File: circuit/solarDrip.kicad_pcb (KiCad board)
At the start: 2 copper layers, 57 x 50 mm, 51 parts, among them J1 solar_charger, J10 Conn_01x08_Socket, J11 Logo_bot, J12 Logo_µc3, J13 solar_charger_smd, J2 batt, J3 solar, J4 pump, J5 soil, J6 water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

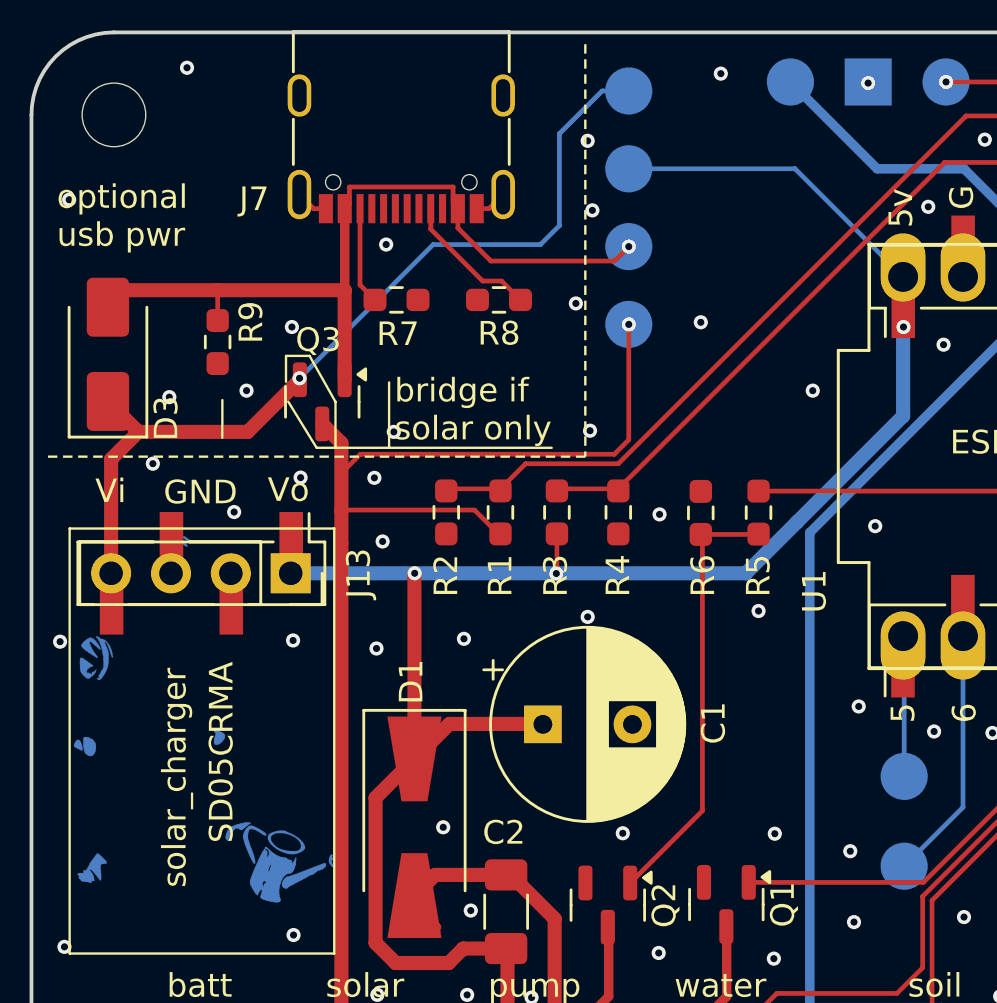
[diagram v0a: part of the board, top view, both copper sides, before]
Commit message: fix usb net
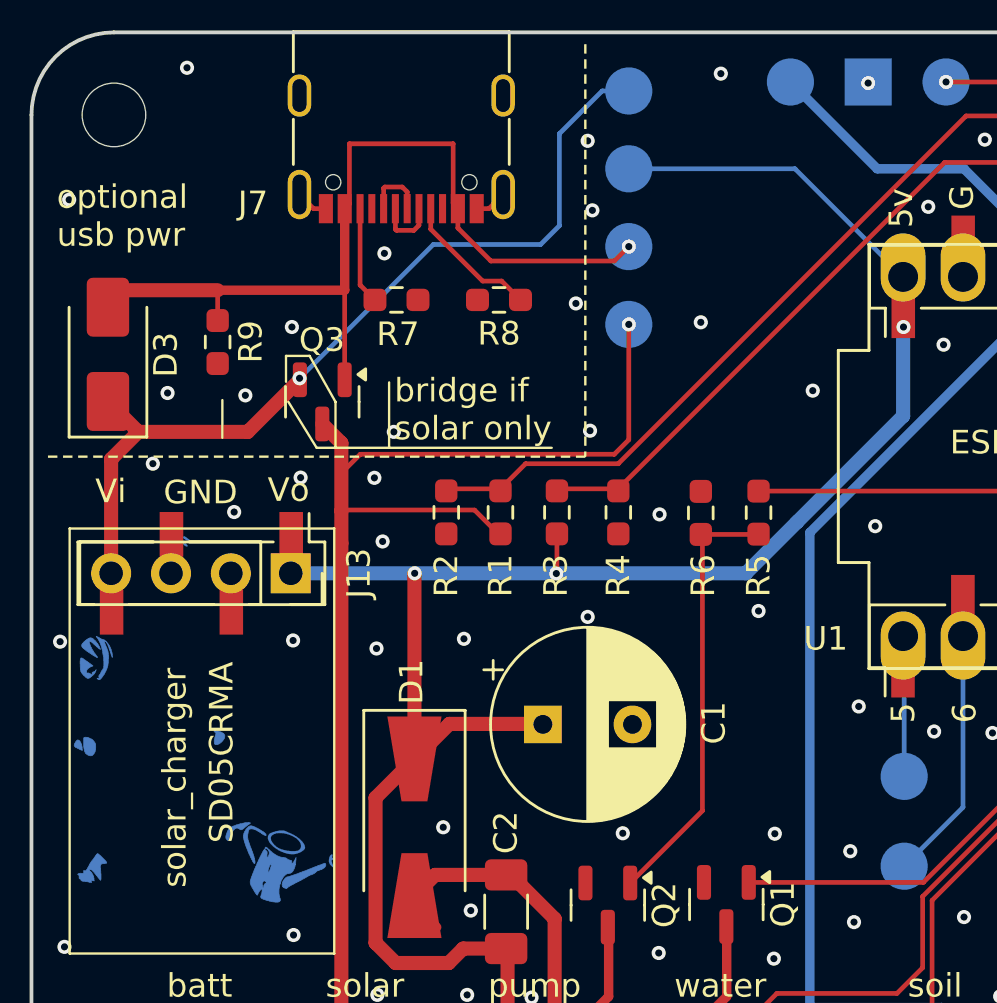
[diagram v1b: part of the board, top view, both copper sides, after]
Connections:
- J7 pad A6: unconnected-(J7-D+-PadA6) -> Net-(J7-D+-PadA6)
- J7 pad A7: unconnected-(J7-D--PadA7) -> Net-(J7-D--PadA7)
- J7 pad B6: unconnected-(J7-D+-PadB6) -> Net-(J7-D+-PadA6)
- J7 pad B7: unconnected-(J7-D--PadB7) -> Net-(J7-D--PadA7)
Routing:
- net vcc_usb: track 34.2 -> 37.9 mm
- net Net-(J7-D+-PadA6): track 0.00 -> 2.69 mm
- net Net-(J7-D--PadA7): track 0.00 -> 2.68 mm
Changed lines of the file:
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@@
 	(net 22 "gpio21")
 	(net 23 "Net-(J7-CC1)")
-	(net 24 "unconnected-(J7-D+-PadA6)")
-	(net 25 "unconnected-(J7-D--PadB7)")
-	(net 26 "unconnected-(J7-D--PadA7)")
-	(net 27 "unconnected-(J7-D+-PadB6)")
-	(net 28 "Net-(J7-CC2)")
+	(net 24 "Net-(J7-D+-PadA6)")
+	(net 25 "Net-(J7-D--PadA7)")
+	(net 26 "Net-(J7-CC2)")
 	(footprint "TestPoint:TestPoint_Pad_2.0x2.0mm"
 		(layer "F.Cu")
@@
 		(tags "SOT TO_SOT_SMD")
 		(property "Reference" "Q3"
-			(at -2.625 0.1642 180)
+			(at -2.625 0.0142 180)
 			(layer "F.SilkS")
 			(effects
@@
 		(property "Value" "pump"
 			(at 1.15 -2.75 0)
-			(layer "F.SilkS")
+			(layer "F.SilkS" knockout)
 			(effects
 				(font
@@
 		(tags "USB C Type-C Receptacle SMD")
 		(property "Reference" "J7"
-			(at 6.242 -3.321 180)
+			(at 6.292 -3.496 180)
 			(layer "F.SilkS")
 			(effects
@@
 			(size 0.3 1.24)
 			(layers "F.Cu" "F.Paste" "F.Mask")
-			(net 24 "unconnected-(J7-D+-PadA6)")
+			(net 24 "Net-(J7-D+-PadA6)")
 			(pinfunction "D+")
-			(pintype "bidirectional+no_connect")
+			(pintype "bidirectional")
 		)
 		(pad "A7" smd rect
@@
 			(size 0.3 1.24)
 			(layers "F.Cu" "F.Paste" "F.Mask")
-			(net 26 "unconnected-(J7-D--PadA7)")
+			(net 25 "Net-(J7-D--PadA7)")
 			(pinfunction "D-")
-			(pintype "bidirectional+no_connect")
+			(pintype "bidirectional")
 		)
 		(pad "A8" smd rect
@@
 			(size 0.3 1.24)
 			(layers "F.Cu" "F.Paste" "F.Mask")
-			(net 28 "Net-(J7-CC2)")
+			(net 26 "Net-(J7-CC2)")
 			(pinfunction "CC2")
 			(pintype "bidirectional")
@@
 			(size 0.3 1.24)
 			(layers "F.Cu" "F.Paste" "F.Mask")
-			(net 27 "unconnected-(J7-D+-PadB6)")
+			(net 24 "Net-(J7-D+-PadA6)")
 			(pinfunction "D+")
-			(pintype "bidirectional+no_connect")
+			(pintype "bidirectional")
 		)
 		(pad "B7" smd rect
@@
 			(size 0.3 1.24)
 			(layers "F.Cu" "F.Paste" "F.Mask")
-			(net 25 "unconnected-(J7-D--PadB7)")
+			(net 25 "Net-(J7-D--PadA7)")
 			(pinfunction "D-")
-			(pintype "bidirectional+no_connect")
+			(pintype "bidirectional")
 		)
 		(pad "B8" smd rect
@@
 		(tags "Diode SMA (DO-214AC)")
 		(property "Reference" "D3"
-			(at -2.715 2.479 90)
+			(at -0.015 2.454 90)
 			(layer "F.SilkS")
 			(effects
@@
 		(tags "resistor handsolder")
 		(property "Reference" "R9"
-			(at -0.8375 -1.425 -90)
+			(at -0.0125 -1.4 -90)
 			(layer "F.SilkS")
 			(effects
@@
 		(at 67.634785 56.468831 90)
 		(property "Reference" "U1"
-			(at -5.715 -13.6525 -90)
+			(at -7.731169 -13.184785 0)
 			(layer "F.SilkS")
 			(effects
@@
 		(tags "capacitor handsolder")
 		(property "Reference" "C2"
-			(at 3.35 -0.09 0)
+			(at 3.36 -0.015 90)
 			(layer "F.SilkS")
 			(effects
@@
 			(layers "F.Cu" "F.Paste" "F.Mask")
 			(roundrect_rratio 0.25)
-			(net 28 "Net-(J7-CC2)")
+			(net 26 "Net-(J7-CC2)")
 			(pintype "passive")
 		)
@@
 	)
 	(via
-		(at 35.8 47.475)
+		(at 35.725 47.85)
 		(size 0.6)
 		(drill 0.3)
@@
 	)
 	(via
-		(at 29.875 53.675)
+		(at 29.825 53.875)
 		(size 0.6)
 		(drill 0.3)
@@
 	)
 	(via
-		(at 26.6 53.95)
+		(at 26.525 53.775)
 		(size 0.6)
 		(drill 0.3)
@@
 	)
 	(segment
-		(start 38.642 45.034)
-		(end 34.242 45.034)
-		(width 0.2)
-		(layer "F.Cu")
-		(net 17)
-	)
-	(segment
-		(start 38.842 45.917)
-		(end 38.642 45.717)
+		(start 34.242 43.2)
+		(end 34.242 45.754)
 		(width 0.2)
 		(layer "F.Cu")
@@
 	)
 	(segment
-		(start 34.242 45.754)
-		(end 34.042 45.954)
+		(start 38.642 45.717)
+		(end 38.642 43.2)
 		(width 0.2)
 		(layer "F.Cu")
@@
 		(start 34.0392 49.4172)
 		(end 34.0392 53.2125)
-		(width 0.6)
+		(width 0.2)
 		(layer "F.Cu")
 		(net 17)
 	)
 	(segment
-		(start 38.842 45.954)
-		(end 38.842 45.917)
+		(start 38.842 45.917)
+		(end 38.642 45.717)
 		(width 0.2)
 		(layer "F.Cu")
@@
 	)
 	(segment
-		(start 38.642 45.717)
-		(end 38.642 45.034)
-		(width 0.2)
-		(layer "F.Cu")
-		(net 17)
-	)
-	(segment
-		(start 34.242 45.034)
-		(end 34.242 45.754)
+		(start 38.642 43.2)
+		(end 34.242 43.2)
 		(width 0.2)
 		(layer "F.Cu")
@@
 		(start 34.042 49.4144)
 		(end 28.65 49.4144)
-		(width 0.6)
+		(width 0.4)
 		(layer "F.Cu")
 		(net 17)
@@
 	)
 	(segment
-		(start 38.842 46.774)
-		(end 38.842 45.954)
+		(start 34.242 45.754)
+		(end 34.042 45.954)
 		(width 0.2)
 		(layer "F.Cu")
@@
 	)
 	(segment
-		(start 34.0392 49.4172)
-		(end 34.042 49.4144)
-		(width 0.6)
+		(start 38.842 45.954)
+		(end 38.842 45.917)
+		(width 0.2)
+		(layer "F.Cu")
+		(net 17)
+	)
+	(segment
+		(start 38.842 46.774)
+		(end 38.842 45.954)
+		(width 0.2)
 		(layer "F.Cu")
 		(net 17)
@@
 	)
 	(segment
+		(start 35.742 45.034)
+		(end 36.484 45.034)
+		(width 0.2)
+		(layer "F.Cu")
+		(net 24)
+	)
+	(segment
+		(start 35.692 45.084)
+		(end 35.742 45.034)
+		(width 0.2)
+		(layer "F.Cu")
+		(net 24)
+	)
+	(segment
+		(start 36.484 45.034)
+		(end 36.692 45.242)
+		(width 0.2)
+		(layer "F.Cu")
+		(net 24)
+	)
+	(segment
+		(start 35.692 45.954)
+		(end 35.692 45.084)
+		(width 0.2)
+		(layer "F.Cu")
+		(net 24)
+	)
+	(segment
+		(start 36.692 45.242)
+		(end 36.692 45.954)
+		(width 0.2)
+		(layer "F.Cu")
+		(net 24)
+	)
+	(segment
+		(start 36.242 46.874)
+		(end 36.976 46.874)
+		(width 0.2)
+		(layer "F.Cu")
+		(net 25)
+	)
+	(segment
+		(start 37.192 46.658)
+		(end 37.192 45.954)
+		(width 0.2)
+		(layer "F.Cu")
+		(net 25)
+	)
+	(segment
+		(start 36.976 46.874)
+		(end 37.192 46.658)
+		(width 0.2)
+		(layer "F.Cu")
+		(net 25)
+	)
+	(segment
+		(start 36.192 45.954)
+		(end 36.192 46.824)
+		(width 0.2)
+		(layer "F.Cu")
+		(net 25)
+	)
+	(segment
+		(start 36.192 46.824)
+		(end 36.242 46.874)
+		(width 0.2)
+		(layer "F.Cu")
+		(net 25)
+	)
+	(segment
 		(start 34.692 49.192)
 		(end 34.692 45.954)
 		(width 0.2)
 		(layer "F.Cu")
-		(net 28)
+		(net 26)
 	)
 	(segment
@@
 		(width 0.2)
 		(layer "F.Cu")
-		(net 28)
+		(net 26)
 	)
 	(zone

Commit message: small improvements
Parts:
- added J14: Logo_oshw, Symbol:OSHW-Logo_5.7x6mm_SilkScreen, B.Cu at (36.4, 42.2)
- added R10: 1K, Resistor_SMD:R_0603_1608Metric_Pad0.98x0.95mm_HandSolder, F.Cu at (55.4, 74.5)
- added R11: 100K, Resistor_SMD:R_0603_1608Metric_Pad0.98x0.95mm_HandSolder, F.Cu at (55.4, 71.7)
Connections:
- Q1 pad 1: out_sensors -> Net-(Q1-G)
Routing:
- net Net-(Q1-G): track 0.00 -> 6.19 mm
- net out_sensors: track 19.6 -> 14.4 mm
- net GND: vias 83 -> 84

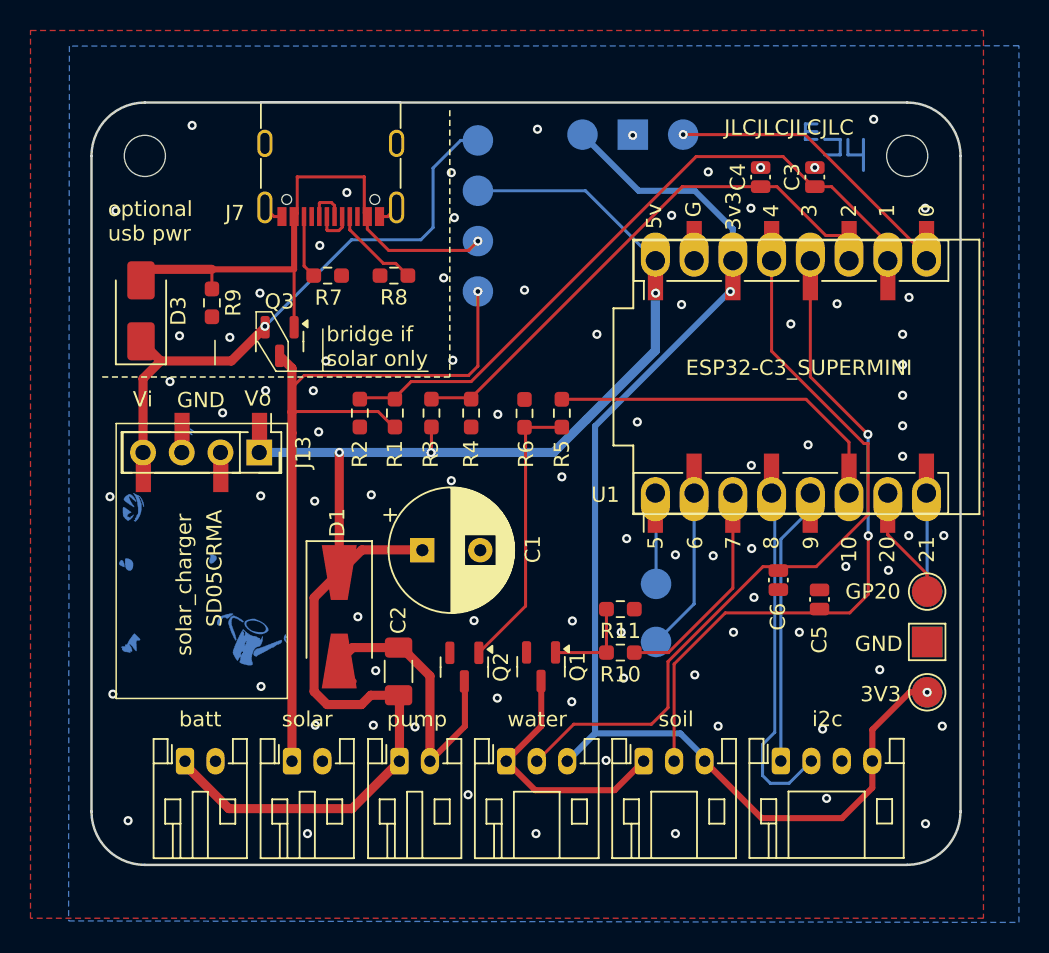
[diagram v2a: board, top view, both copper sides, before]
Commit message: change caps to 0603
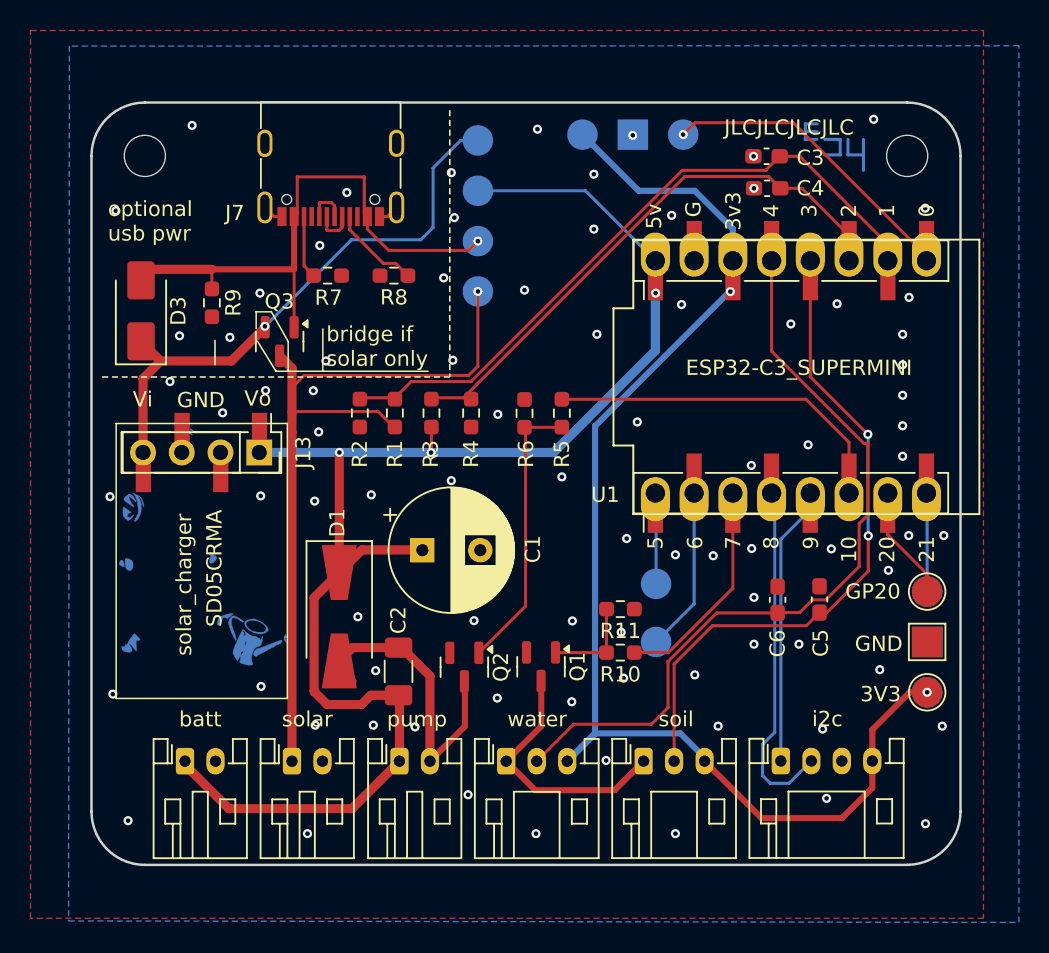
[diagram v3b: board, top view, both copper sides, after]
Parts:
- C3, C4, C5, C6: footprint Capacitor_SMD:C_0504_1310Metric_Pad0.83x1.28mm_HandSolder -> Capacitor_SMD:C_0603_1608Metric_Pad1.08x0.95mm_HandSolder
- moved C3 3.45 mm to (65.0, 42.0), turned to 180 degrees
- moved C6 1.29 mm to (65.8, 71.1), turned to 90 degrees
- moved C4 0.85 mm to (65.1, 44.1), turned to 180 degrees
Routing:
- net in-a_water: track 49.6 -> 51.3 mm
- net solar_hi: track 46.0 -> 47.1 mm
- net in-a_moisture: track 44.5 -> 43.6 mm
- net gpio0: track 19.6 -> 20.2 mm
